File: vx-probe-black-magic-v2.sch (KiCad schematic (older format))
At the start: 18 parts, among them P1 USB MINI B, U1 stm32f070-qfp48, U2 AT45DB321D-SU, Y1 8 MHz

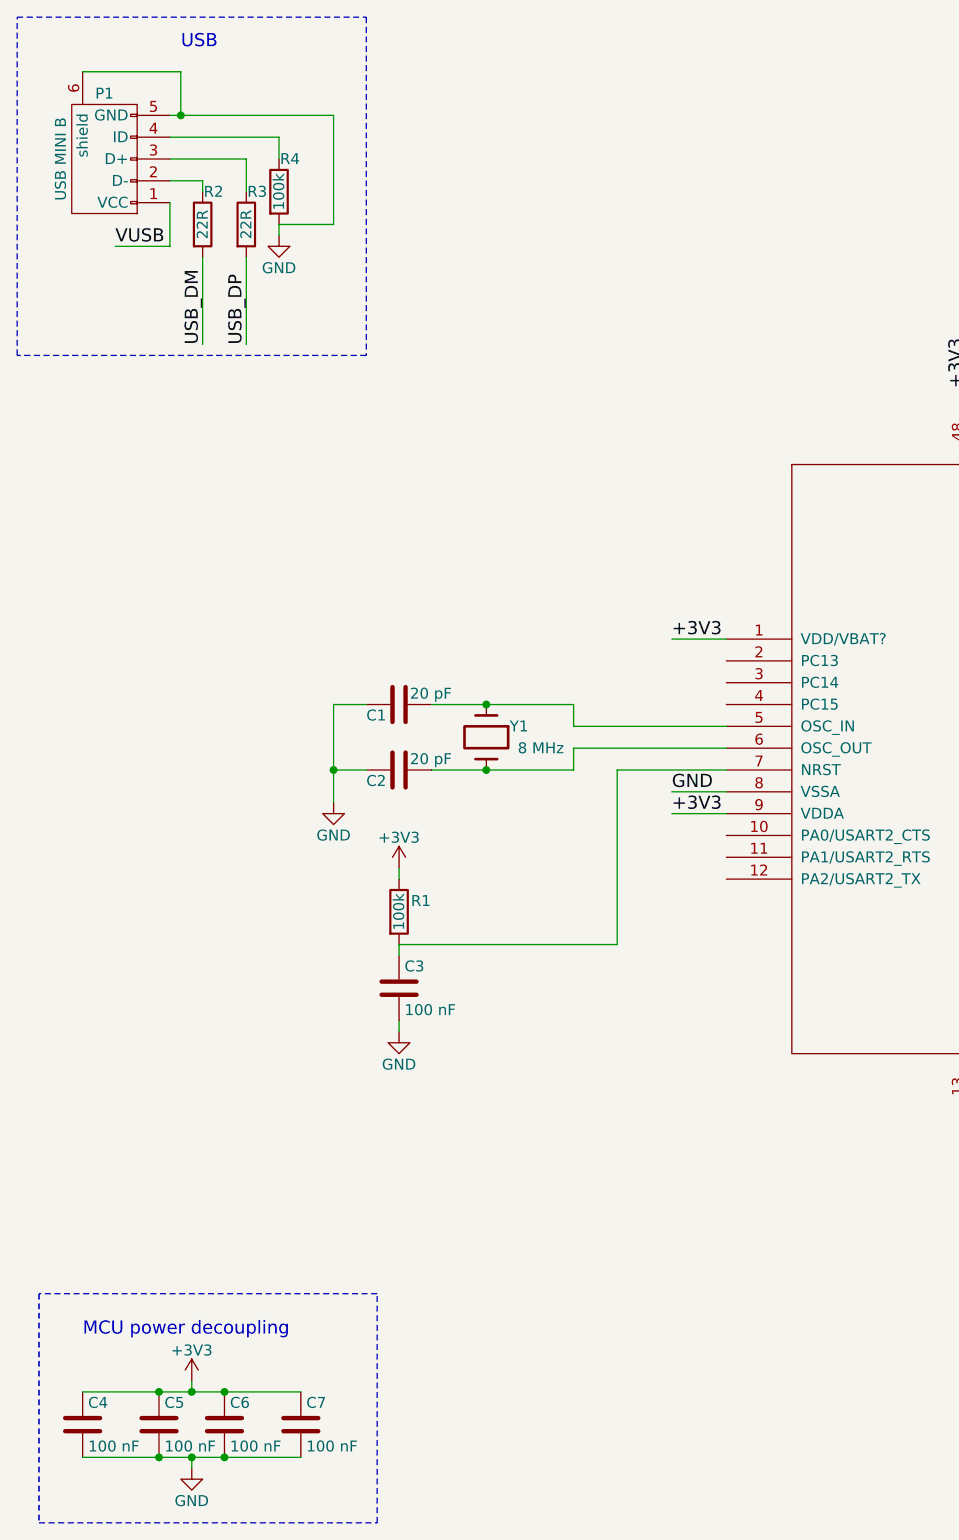
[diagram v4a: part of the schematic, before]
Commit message: added missing pull-up resistor on the usb-data-plus line
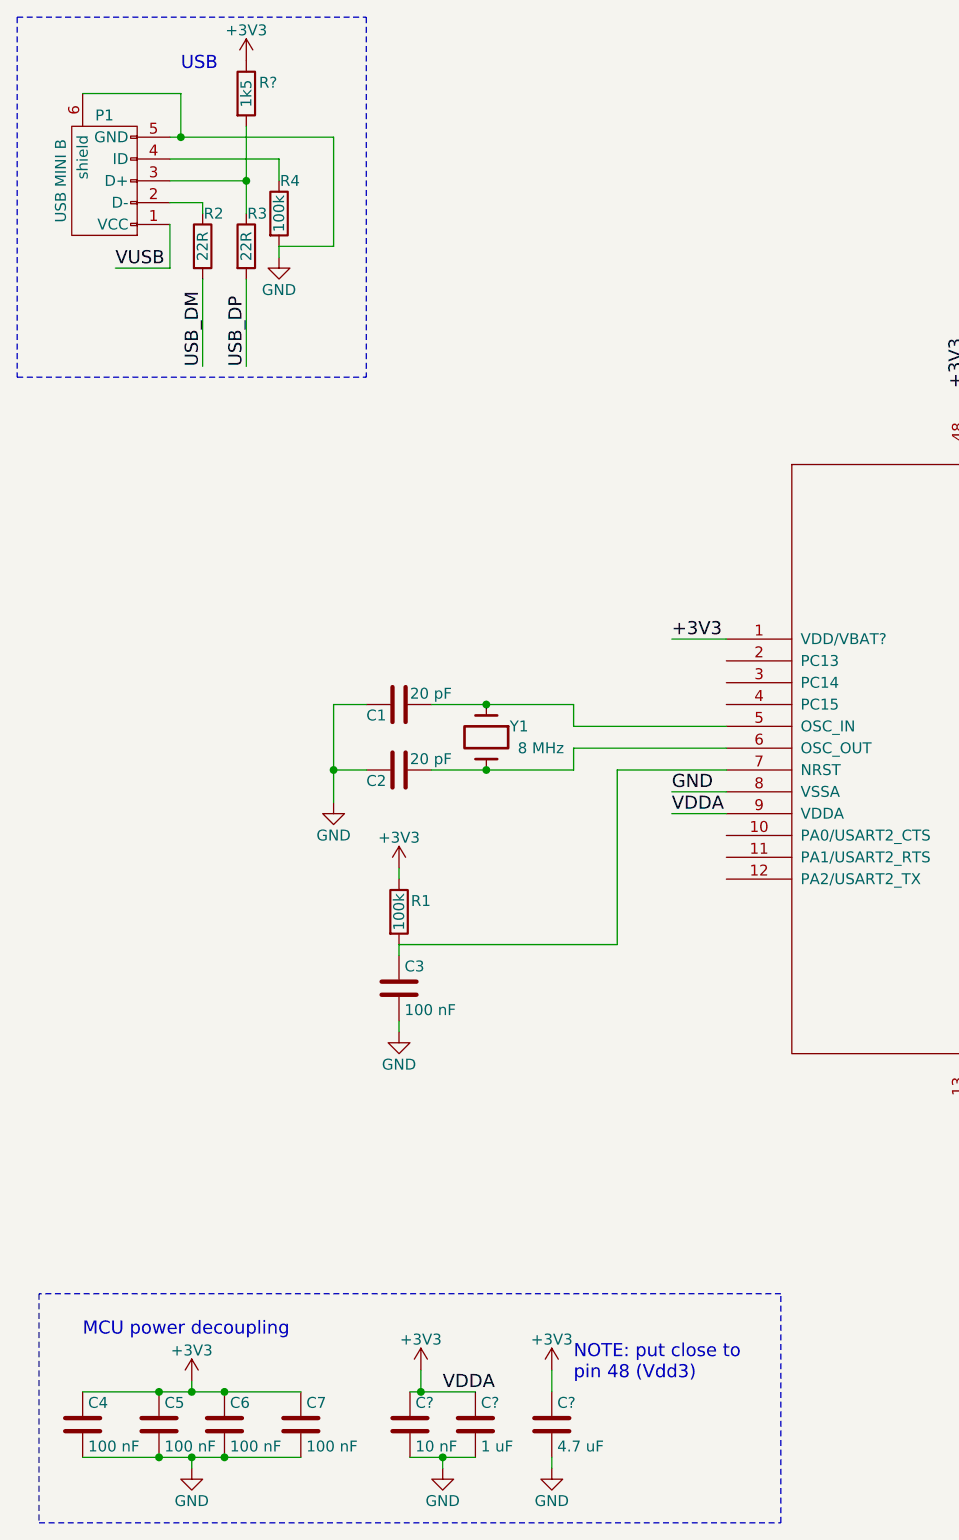
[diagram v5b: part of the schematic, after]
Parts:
- added C?: 10 nF, symbol C
- added C?: 1 uF, symbol C
- added C?: 4.7 uF, symbol C
- added R?: 1k5, symbol R
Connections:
- net labels added: VDDA
- wire segments 76 -> 82
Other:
- note added: "NOTE: put close to\npin 48 (Vdd3)"
- moved on the sheet: P1, R2, R3, R4
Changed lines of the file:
@@
 	1    0    0    -1
 $EndComp
-Text Label 3750 4250 0    60   ~ 0
-+3V3
 Text Label 3750 4150 0    60   ~ 0
 GND
@@
 L USB_OTG P1
 U 1 1 57D82DC6
-P 1150 1250
-F 0 "P1" V 1450 1250 50  0000 C CNN
-F 1 "USB MINI B" H 1150 1450 50  0000 C CNN
-F 2 "Connect:USB_Mini-B" V 1100 1150 50  0001 C CNN
-F 3 "" V 1100 1150 50  0000 C CNN
-	1    1150 1250
+P 1150 1350
+F 0 "P1" V 1450 1350 50  0000 C CNN
+F 1 "USB MINI B" H 1150 1550 50  0000 C CNN
+F 2 "Connect:USB_Mini-B" V 1100 1250 50  0001 C CNN
+F 3 "" V 1100 1250 50  0000 C CNN
+	1    1150 1350
 	0    -1   -1   0
 $EndComp
@@
 L R R4
 U 1 1 57D831E6
-P 1950 1400
-F 0 "R4" H 2000 1550 50  0000 C CNN
-F 1 "100k" V 1950 1400 50  0000 C CNN
-F 2 "Resistors_SMD:R_0805" H 2150 1300 50  0001 C CNN
-F 3 "" H 1950 1400 50  0000 C CNN
-	1    1950 1400
+P 1950 1500
+F 0 "R4" H 2000 1650 50  0000 C CNN
+F 1 "100k" V 1950 1500 50  0000 C CNN
+F 2 "Resistors_SMD:R_0805" H 2150 1400 50  0001 C CNN
+F 3 "" H 1950 1500 50  0000 C CNN
+	1    1950 1500
 	1    0    0    -1
 $EndComp
@@
 L GND #PWR06
 U 1 1 57D8325D
-P 1950 1600
-F 0 "#PWR06" H 1950 1350 50  0001 C CNN
-F 1 "GND" H 1950 1450 50  0000 C CNN
-F 2 "" H 1950 1600 50  0000 C CNN
-F 3 "" H 1950 1600 50  0000 C CNN
-	1    1950 1600
+P 1950 1700
+F 0 "#PWR06" H 1950 1450 50  0001 C CNN
+F 1 "GND" H 1950 1550 50  0000 C CNN
+F 2 "" H 1950 1700 50  0000 C CNN
+F 3 "" H 1950 1700 50  0000 C CNN
+	1    1950 1700
 	1    0    0    -1
 $EndComp
@@
 L R R3
 U 1 1 57D83361
-P 1800 1550
-F 0 "R3" H 1850 1700 50  0000 C CNN
-F 1 "22R" V 1800 1550 50  0000 C CNN
-F 2 "Resistors_SMD:R_0805" V 1730 1550 50  0001 C CNN
-F 3 "" H 1800 1550 50  0000 C CNN
-	1    1800 1550
+P 1800 1650
+F 0 "R3" H 1850 1800 50  0000 C CNN
+F 1 "22R" V 1800 1650 50  0000 C CNN
+F 2 "Resistors_SMD:R_0805" V 1730 1650 50  0001 C CNN
+F 3 "" H 1800 1650 50  0000 C CNN
+	1    1800 1650
 	1    0    0    -1
 $EndComp
@@
 L R R2
 U 1 1 57D833EA
-P 1600 1550
-F 0 "R2" H 1650 1700 50  0000 C CNN
-F 1 "22R" V 1600 1550 50  0000 C CNN
-F 2 "Resistors_SMD:R_0805" V 1530 1550 50  0001 C CNN
-F 3 "" H 1600 1550 50  0000 C CNN
-	1    1600 1550
-	1    0    0    -1
-$EndComp
-Text Label 1200 1650 0    60   ~ 0
+P 1600 1650
+F 0 "R2" H 1650 1800 50  0000 C CNN
+F 1 "22R" V 1600 1650 50  0000 C CNN
+F 2 "Resistors_SMD:R_0805" V 1530 1650 50  0001 C CNN
+F 3 "" H 1600 1650 50  0000 C CNN
+	1    1600 1650
+	1    0    0    -1
+$EndComp
+Text Label 1200 1750 0    60   ~ 0
 VUSB
-Text Label 1600 2100 1    60   ~ 0
+Text Label 1600 2200 1    60   ~ 0
 USB_DM
-Text Label 1800 2100 1    60   ~ 0
+Text Label 1800 2200 1    60   ~ 0
 USB_DP
 Text Label 7350 3750 0    60   ~ 0
@@
 Text Label 7350 3850 0    60   ~ 0
 USB_DM
-Text Notes 1500 750  0    60   ~ 0
+Text Notes 1500 850  0    60   ~ 0
 USB
 $Comp
@@
 	850  6450 850  7500
 Wire Notes Line
-	850  7500 2400 7500
-Wire Notes Line
-	2400 7500 2400 6450
-Wire Notes Line
-	2400 6450 850  6450
-Wire Wire Line
-	1450 1050 2200 1050
-Wire Wire Line
-	1050 850  1500 850
-Wire Wire Line
-	1500 850  1500 1050
-Connection ~ 1500 1050
-Wire Wire Line
-	1450 1150 1950 1150
-Wire Wire Line
-	1950 1150 1950 1250
-Wire Wire Line
-	1950 1550 1950 1600
-Wire Wire Line
-	2200 1050 2200 1550
-Wire Wire Line
-	2200 1550 1950 1550
-Wire Wire Line
-	1450 1250 1800 1250
-Wire Wire Line
-	1800 1250 1800 1400
-Wire Wire Line
-	1450 1350 1600 1350
-Wire Wire Line
-	1600 1350 1600 1400
-Wire Wire Line
-	1450 1450 1450 1650
-Wire Wire Line
-	1450 1650 1200 1650
-Wire Wire Line
-	1600 1700 1600 2100
-Wire Wire Line
-	1800 1700 1800 2100
+	850  7500 4250 7500
+Wire Notes Line
+	4250 7500 4250 6450
+Wire Notes Line
+	4250 6450 850  6450
+Wire Wire Line
+	1450 1150 2200 1150
+Wire Wire Line
+	1050 950  1500 950
+Wire Wire Line
+	1500 950  1500 1150
+Connection ~ 1500 1150
+Wire Wire Line
+	1450 1250 1950 1250
+Wire Wire Line
+	1950 1250 1950 1350
+Wire Wire Line
+	1950 1650 1950 1700
+Wire Wire Line
+	2200 1150 2200 1650
+Wire Wire Line
+	2200 1650 1950 1650
+Wire Wire Line
+	1450 1350 1800 1350
+Wire Wire Line
+	1800 1100 1800 1500
+Wire Wire Line
+	1450 1450 1600 1450
+Wire Wire Line
+	1600 1450 1600 1500
+Wire Wire Line
+	1450 1550 1450 1750
+Wire Wire Line
+	1450 1750 1200 1750
+Wire Wire Line
+	1600 1800 1600 2200
+Wire Wire Line
+	1800 1800 1800 2200
 Wire Wire Line
 	7300 3750 7700 3750
@@
 	750  600  2350 600
 Wire Notes Line
-	2350 600  2350 2150
-Wire Notes Line
-	2350 2150 750  2150
-Wire Notes Line
-	750  2150 750  600
+	2350 600  2350 2250
+Wire Notes Line
+	750  2250 2350 2250
+Wire Notes Line
+	750  600  750  2250
 Wire Wire Line
 	10800 1150 10450 1150
@@
 Text Label 6100 2250 1    60   ~ 0
 UEXT_SSEL
+Text Label 3750 4250 0    60   ~ 0
+VDDA
+$Comp
+L C C?
+U 1 1 57D889A2
+P 2550 7050
+F 0 "C?" H 2575 7150 50  0000 L CNN
+F 1 "10 nF" H 2575 6950 50  0000 L CNN
+F 2 "" H 2588 6900 50  0000 C CNN
+F 3 "" H 2550 7050 50  0000 C CNN
+	1    2550 7050
+	1    0    0    -1
+$EndComp
+$Comp
+L C C?
+U 1 1 57D88A0C
+P 2850 7050
+F 0 "C?" H 2875 7150 50  0000 L CNN
+F 1 "1 uF" H 2875 6950 50  0000 L CNN
+F 2 "" H 2888 6900 50  0000 C CNN
+F 3 "" H 2850 7050 50  0000 C CNN
+	1    2850 7050
+	1    0    0    -1
+$EndComp
+Wire Wire Line
+	2550 6900 2850 6900
+Wire Wire Line
+	2850 7200 2550 7200
+Wire Wire Line
+	2700 7200 2700 7250
+Connection ~ 2700 7200
+$Comp
+L GND #PWR?
+U 1 1 57D88BF4
+P 2700 7250
+F 0 "#PWR?" H 2700 7000 50  0001 C CNN
+F 1 "GND" H 2700 7100 50  0000 C CNN
+F 2 "" H 2700 7250 50  0000 C CNN
+F 3 "" H 2700 7250 50  0000 C CNN
+	1    2700 7250
+	1    0    0    -1
+$EndComp
+Wire Wire Line
+	2600 6900 2600 6800
+Connection ~ 2600 6900
+$Comp
+L +3V3 #PWR?
+U 1 1 57D88CB2
+P 2600 6800
+F 0 "#PWR?" H 2600 6650 50  0001 C CNN
+F 1 "+3V3" H 2600 6940 50  0000 C CNN
+F 2 "" H 2600 6800 50  0000 C CNN
+F 3 "" H 2600 6800 50  0000 C CNN
+	1    2600 6800
+	1    0    0    -1
+$EndComp
+Text Label 2700 6900 0    60   ~ 0
+VDDA
+$Comp
+L C C?
+U 1 1 57D88F0B
+P 3200 7050
+F 0 "C?" H 3225 7150 50  0000 L CNN
+F 1 "4.7 uF" H 3225 6950 50  0000 L CNN
+F 2 "" H 3238 6900 50  0000 C CNN
+F 3 "" H 3200 7050 50  0000 C CNN
+	1    3200 7050
+	1    0    0    -1
+$EndComp
+Wire Wire Line
+	3200 7200 3200 7250
+$Comp
+L GND #PWR?
+U 1 1 57D88FD9
+P 3200 7250
+F 0 "#PWR?" H 3200 7000 50  0001 C CNN
+F 1 "GND" H 3200 7100 50  0000 C CNN
+F 2 "" H 3200 7250 50  0000 C CNN
+F 3 "" H 3200 7250 50  0000 C CNN
+	1    3200 7250
+	1    0    0    -1
+$EndComp
+Wire Wire Line
+	3200 6900 3200 6800
+$Comp
+L +3V3 #PWR?
+U 1 1 57D890F4
+P 3200 6800
+F 0 "#PWR?" H 3200 6650 50  0001 C CNN
+F 1 "+3V3" H 3200 6940 50  0000 C CNN
+F 2 "" H 3200 6800 50  0000 C CNN
+F 3 "" H 3200 6800 50  0000 C CNN
+	1    3200 6800
+	1    0    0    -1
+$EndComp
+Text Notes 3300 6850 0    60   ~ 0
+NOTE: put close to\npin 48 (Vdd3)
+Connection ~ 1800 1350
+$Comp
+L R R?
+U 1 1 57D89DD6
+P 1800 950
+F 0 "R?" H 1900 1000 50  0000 C CNN
+F 1 "1k5" V 1800 950 50  0000 C CNN
+F 2 "" V 1730 950 50  0000 C CNN
+F 3 "" H 1800 950 50  0000 C CNN
+	1    1800 950
+	1    0    0    -1
+$EndComp
+$Comp
+L +3V3 #PWR?
+U 1 1 57D89E25
+P 1800 800
+F 0 "#PWR?" H 1800 650 50  0001 C CNN
+F 1 "+3V3" H 1800 940 50  0000 C CNN
+F 2 "" H 1800 800 50  0000 C CNN
+F 3 "" H 1800 800 50  0000 C CNN
+	1    1800 800
+	1    0    0    -1
+$EndComp
 $EndSCHEMATC

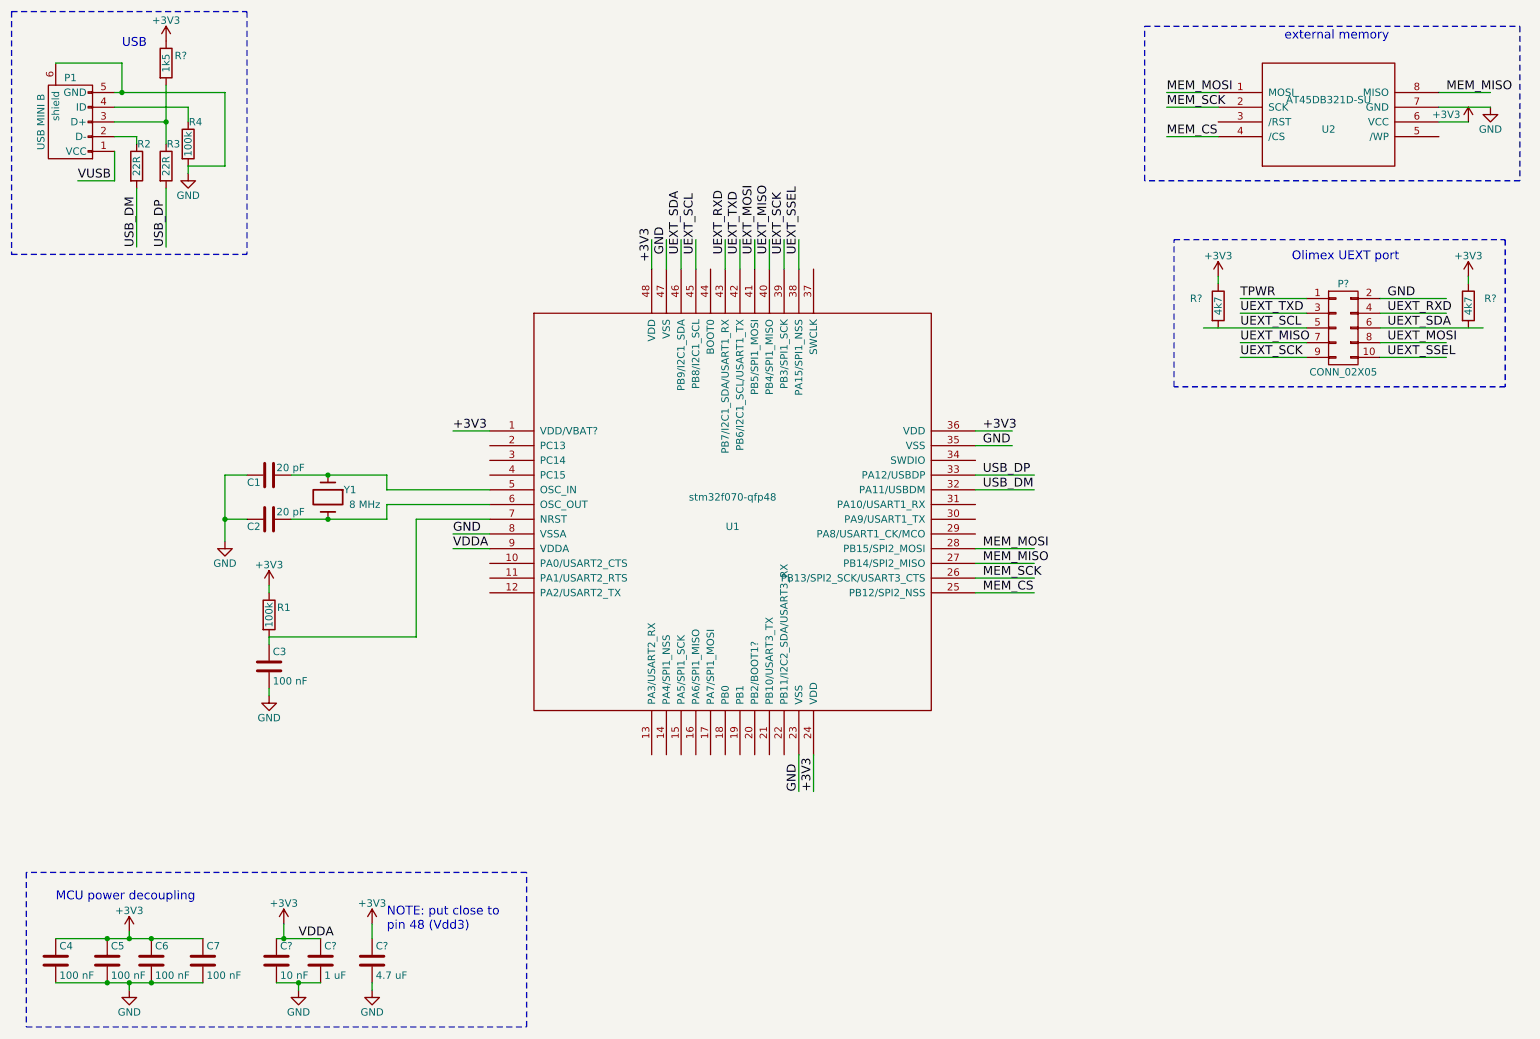
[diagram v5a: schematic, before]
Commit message: added serial wire debug/programming header
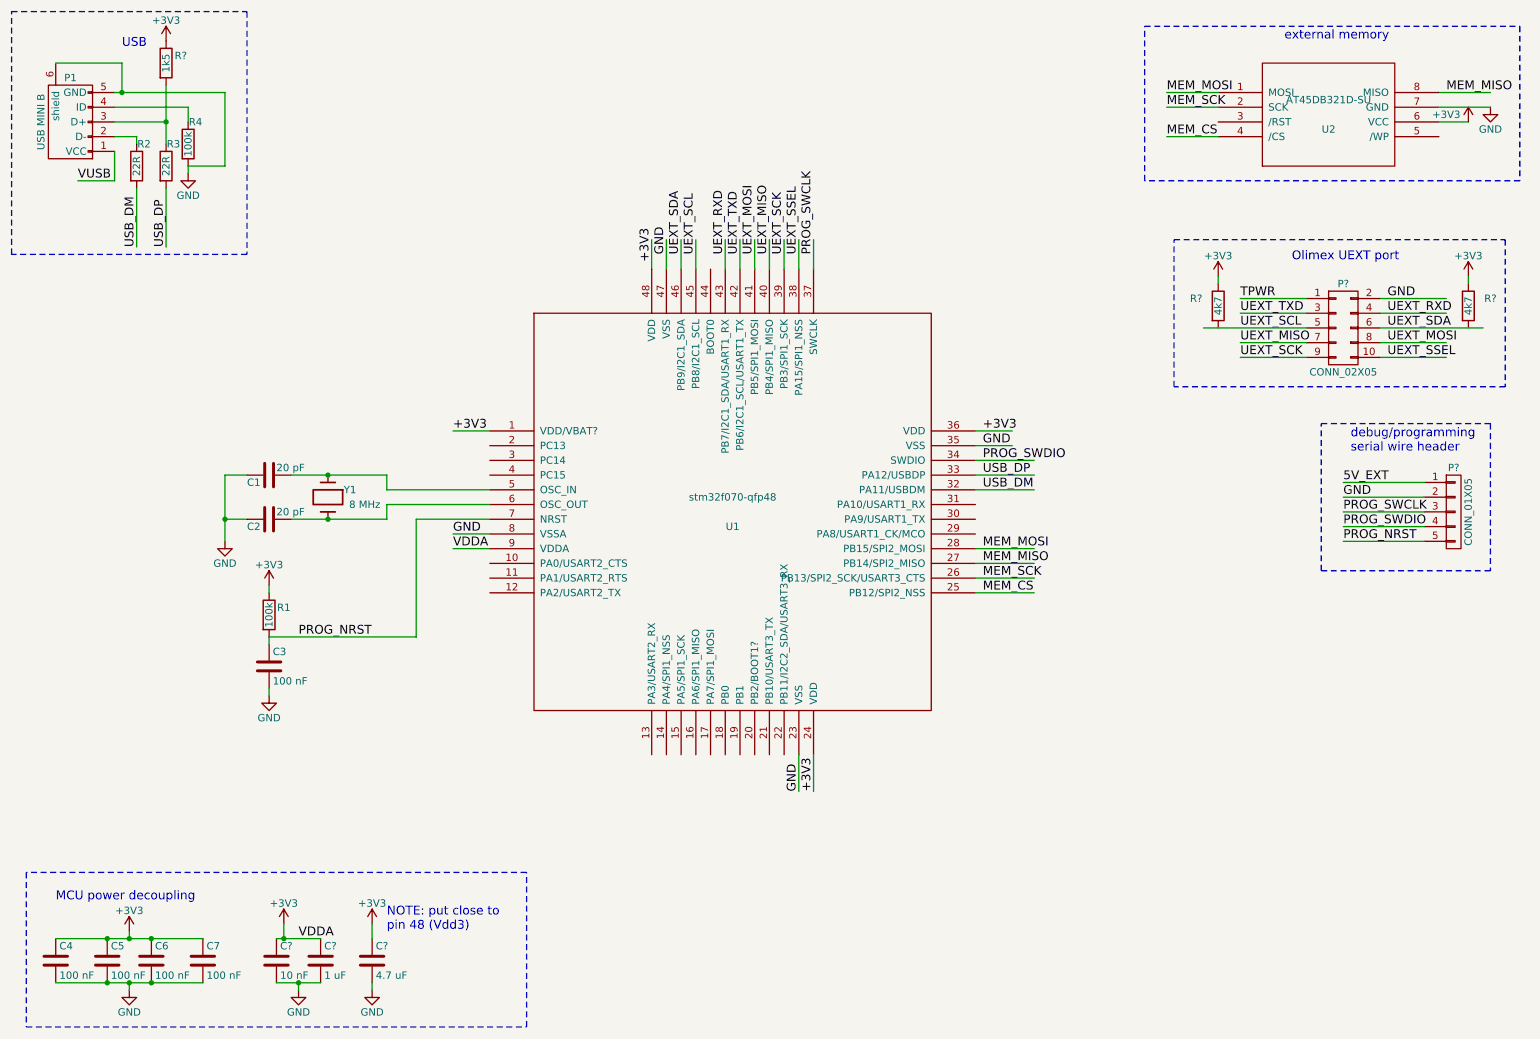
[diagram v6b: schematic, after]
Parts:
- added P?: CONN_01X05, symbol CONN_01X05
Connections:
- net labels added: 5V_EXT, PROG_NRST, PROG_SWCLK, PROG_SWDIO
- wire segments 82 -> 89
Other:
- note added: "debug/programming\nserial wire header"
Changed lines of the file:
@@
 	2350 600  2350 2250
 Wire Notes Line
-	750  2250 2350 2250
-Wire Notes Line
-	750  600  750  2250
+	2350 2250 750  2250
+Wire Notes Line
+	750  2250 750  600
 Wire Wire Line
 	10800 1150 10450 1150
@@
 	1    0    0    -1
 $EndComp
+Text Label 2700 4850 0    60   ~ 0
+PROG_NRST
+Wire Wire Line
+	7300 3650 7700 3650
+Text Label 7350 3650 0    60   ~ 0
+PROG_SWDIO
+Wire Wire Line
+	6200 2350 6200 2150
+Text Label 6200 2250 1    60   ~ 0
+PROG_SWCLK
+$Comp
+L CONN_01X05 P?
+U 1 1 57D8BC7C
+P 10550 4000
+F 0 "P?" H 10550 4300 50  0000 C CNN
+F 1 "CONN_01X05" V 10650 4000 50  0000 C CNN
+F 2 "" H 10550 4000 50  0000 C CNN
+F 3 "" H 10550 4000 50  0000 C CNN
+	1    10550 4000
+	1    0    0    -1
+$EndComp
+Wire Wire Line
+	9800 3800 10350 3800
+Wire Wire Line
+	9800 3900 10350 3900
+Wire Wire Line
+	9800 4000 10350 4000
+Wire Wire Line
+	9800 4100 10350 4100
+Wire Wire Line
+	9800 4200 10350 4200
+Text Label 9800 3800 0    60   ~ 0
+5V_EXT
+Text Label 9800 3900 0    60   ~ 0
+GND
+Text Label 9800 4000 0    60   ~ 0
+PROG_SWCLK
+Text Label 9800 4100 0    60   ~ 0
+PROG_SWDIO
+Text Label 9800 4200 0    60   ~ 0
+PROG_NRST
+Text Notes 9850 3600 0    60   ~ 0
+debug/programming\nserial wire header
+Wire Notes Line
+	9650 3400 10800 3400
+Wire Notes Line
+	10800 3400 10800 4400
+Wire Notes Line
+	10800 4400 9650 4400
+Wire Notes Line
+	9650 4400 9650 3400
 $EndSCHEMATC
